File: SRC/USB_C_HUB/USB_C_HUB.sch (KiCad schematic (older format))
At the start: 44 parts, among them J1 USB_C_Receptacle, J2 USB3_A, J3 USB3_A, J4 USB_C_Receptacle, P1 USB_C_Plug, P2 USB_C_Plug_USB2.0, U1 HD3SS460, U2 SY6280, U3 SY6280, U4 SY6280, U5 SY6280

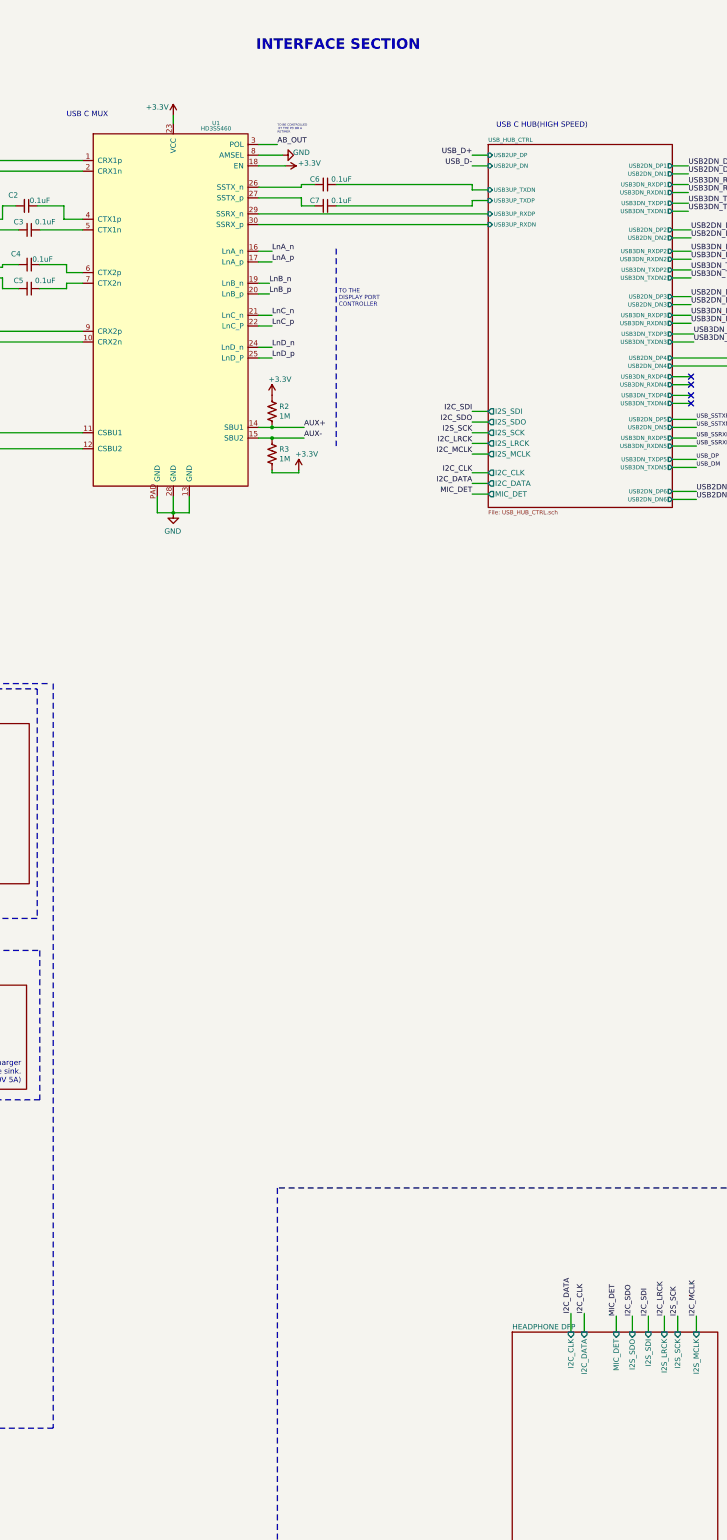
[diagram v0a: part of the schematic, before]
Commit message: schematic capture complete. Pending FULL Footprint assignment. accetable warnings=21
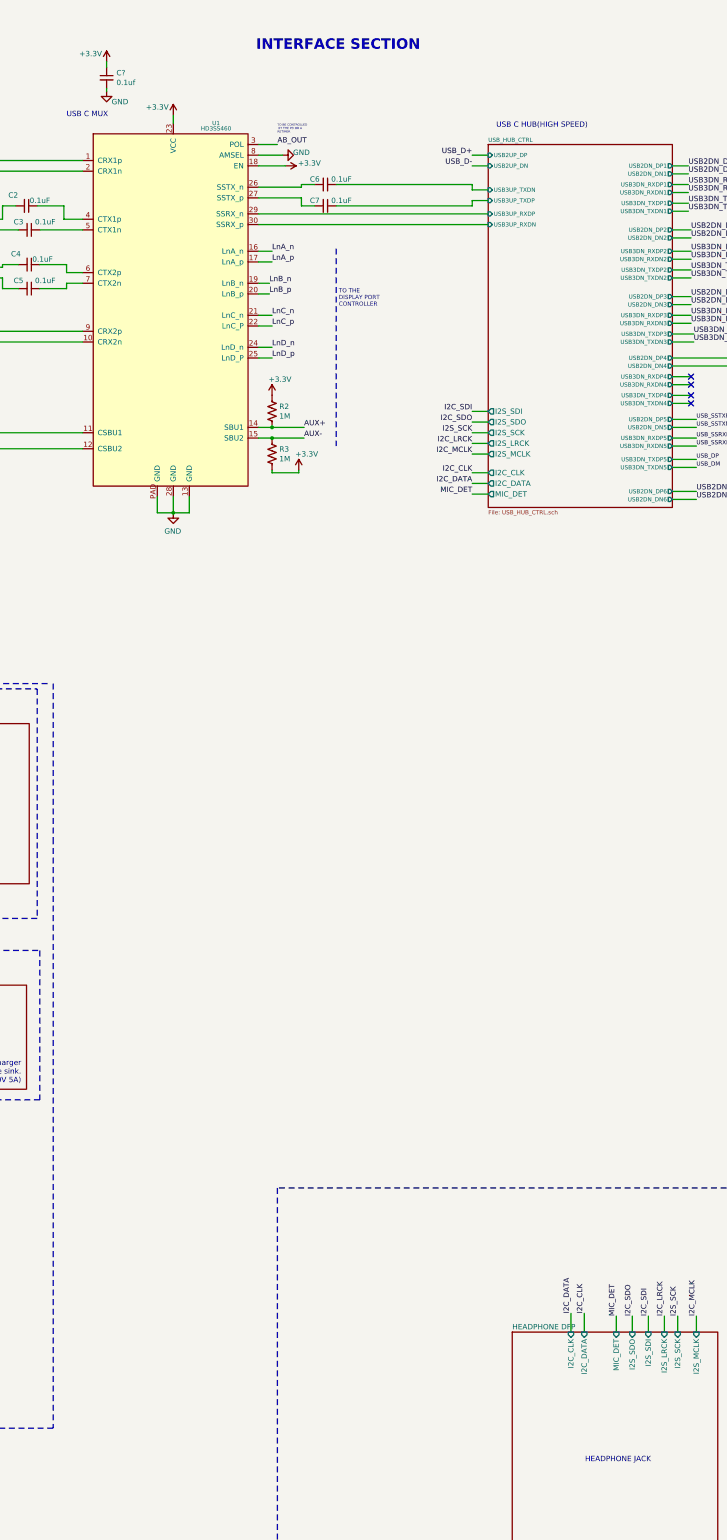
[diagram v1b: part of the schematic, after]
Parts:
- added C?: 0.1uf, symbol Device:C_Small
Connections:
- net +3V3: now also C?.1
- net GND: now also C?.2
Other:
- note added: "HEADPHONE JACK\n"
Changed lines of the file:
@@
 encoding utf-8
 Sheet 1 15
-Title ""
-Date ""
-Rev ""
+Title "USB C HUB"
+Date "2021-10-28"
+Rev "1.1"
 Comp ""
-Comment1 ""
+Comment1 "Designer: ROBERT M M"
 Comment2 ""
 Comment3 ""
@@
 Wire Notes Line
 	15650 525  15650 11575
+$Comp
+L Device:C_Small C?
+U 1 1 64CB2E8E
+P 6425 1175
+F 0 "C?" H 6517 1221 50  0000 L CNN
+F 1 "0.1uf" H 6517 1130 50  0000 L CNN
+F 2 "" H 6425 1175 50  0001 C CNN
+F 3 "~" H 6425 1175 50  0001 C CNN
+	1    6425 1175
+	1    0    0    -1
+$EndComp
+$Comp
+L OLIMEX_Power:+3.3V #PWR?
+U 1 1 64CB3D37
+P 6425 1025
+F 0 "#PWR?" H 6425 875 50  0001 C CNN
+F 1 "+3.3V" H 6275 1100 50  0000 C CNN
+F 2 "" H 6425 1025 60  0000 C CNN
+F 3 "" H 6425 1025 60  0000 C CNN
+	1    6425 1025
+	1    0    0    -1
+$EndComp
+$Comp
+L OLIMEX_Power:GND #PWR?
+U 1 1 64CDC8A5
+P 6425 1300
+AR Path="/619540C6/64CDC8A5" Ref="#PWR?"  Part="1"
+AR Path="/64CDC8A5" Ref="#PWR?"  Part="1"
+F 0 "#PWR?" H 6425 1050 50  0001 C CNN
+F 1 "GND" H 6300 1200 50  0000 C CNN
+F 2 "" H 6425 1300 60  0000 C CNN
+F 3 "" H 6425 1300 60  0000 C CNN
+	1    6425 1300
+	-1   0    0    -1
+$EndComp
+Wire Wire Line
+	6425 1025 6425 1075
+Wire Wire Line
+	6425 1275 6425 1300
+Text Notes 11525 14150 2    50   ~ 0
+HEADPHONE JACK\n
 $EndSCHEMATC

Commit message: schematic capture and footprint assignment complete. Pending approval
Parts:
- removed P2: USB_C_Plug_USB2.0, symbol Connector:USB_C_Plug_USB2.0
- added J10: USB_C_Receptacle_USB2.0, footprints:GCT_USB4105_REVA, symbol Connector:USB_C_Receptacle_USB2.0
- C1, C12: footprint (none) -> Capacitor_SMD:C_0402_1005Metric; Mfr No. (none) -> 0402B104K6R3CT
- C10, C11, C13, C17, C19, C8: footprint (none) -> Capacitor_SMD:C_0603_1608Metric
- C14, C16, C18, C2, C3, C4, C5, C6, C7: footprint (none) -> Capacitor_SMD:C_0402_1005Metric
- C15, C9: footprint (none) -> Capacitor_SMD:C_0603_1608Metric; Mfr No. (none) -> CL10A106MQ8NNNC
- C203: renamed from C?; footprint (none) -> Capacitor_SMD:C_0402_1005Metric
- J1: footprint (none) -> Connector_USB:USB_C_Receptacle_Amphenol_12401610E4-2A
- J2, J3: footprint (none) -> footprints:USB_A_3.1_GCT_USB1075-XX-X-X_REVE
- J4: footprint (none) -> footprints:usb_C_MOLEX_105450-0101
- P1: footprint (none) -> footprints:USB_C_PLUG_GCT_USB4155-03-C_REVA
- R1: value R_US -> 1K; footprint (none) -> Resistor_SMD:R_0402_1005Metric; Mfr No. (none) -> 0402WGF1001TCE
- R2: footprint (none) -> Resistor_SMD:R_0402_1005Metric; Mfr No, (none) -> 0402WGF1004TCE
- R3: footprint (none) -> Resistor_SMD:R_0402_1005Metric
- R4: footprint (none) -> Resistor_SMD:R_0603_1608Metric; Mfr No. (none) -> AS03W4J0682T5E
- R5, R6, R7: footprint (none) -> Resistor_SMD:R_0603_1608Metric
- U1: footprint (none) -> footprints:QFN40P450X250X80-31N120X320
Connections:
- net GND: now also J10.A1 (GND), J10.A12 (GND), J10.B1 (GND), J10.B12 (GND), J10.S1 (SHIELD)
- net USB2DN_DN6: now also J10.A7 (D-)
- net USB2DN_DP6: now also J10.A6 (D+)
- net at C13.1, C18.1, U2.1 (OUT): now also J10.A4 (VBUS), J10.A9 (VBUS), J10.B4 (VBUS), J10.B9 (VBUS)
- no-connect marks 30 -> 32

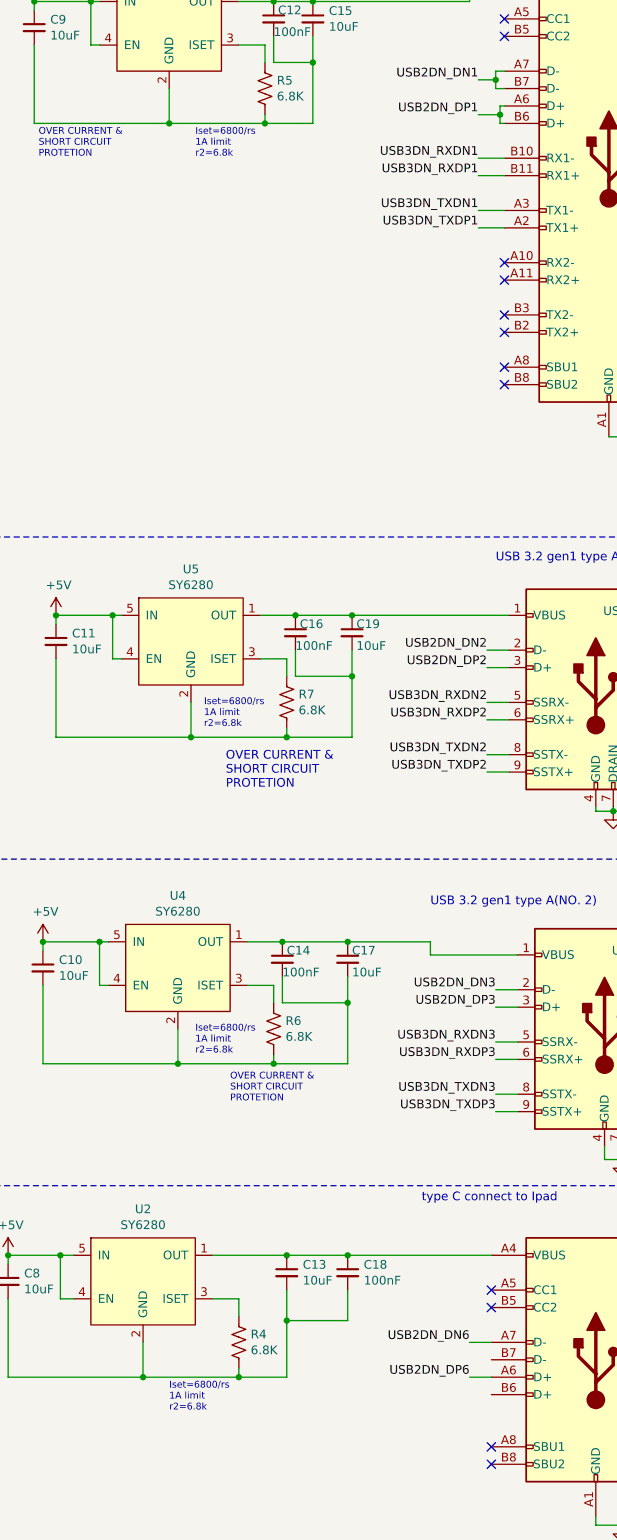
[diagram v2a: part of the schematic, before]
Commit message: schematic capture and footprint assignment complete.
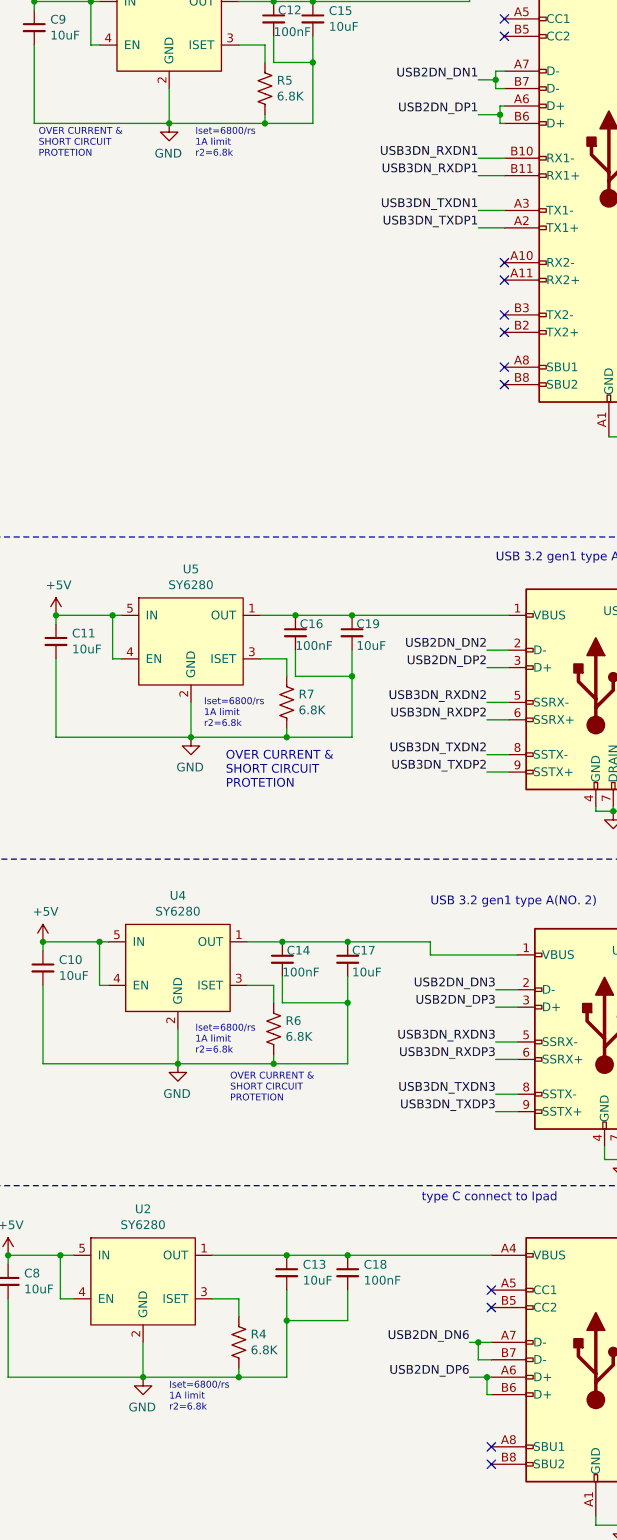
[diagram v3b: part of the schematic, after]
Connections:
- net GND: now also C10.2, C11.2, C12.2, C13.2, C14.2, C15.2, C16.2, C17.2, C18.2, C19.2, C8.2, C9.2, R4.2, R5.2, R6.2, R7.2, U2.2 (GND), U3.2 (GND), U4.2 (GND), U5.2 (GND)
- net USB2DN_DN6: now also J10.B7 (D-)
- net USB2DN_DP6: now also J10.B6 (D+)
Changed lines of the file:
@@
 USB2DN_DN6
 Wire Wire Line
-	21425 8650 21300 8650
-Wire Wire Line
-	21425 8850 21300 8850
+	21425 8650 21350 8650
 NoConn ~ 21425 8450
 NoConn ~ 21425 8350
@@
 NoConn ~ 21425 9250
 NoConn ~ 21425 9350
+$Comp
+L OLIMEX_Power:GND #PWR?
+U 1 1 617FB915
+P 19575 1650
+AR Path="/619540C6/617FB915" Ref="#PWR?"  Part="1"
+AR Path="/617FB915" Ref="#PWR0206"  Part="1"
+F 0 "#PWR0206" H 19575 1400 50  0001 C CNN
+F 1 "GND" H 19580 1477 50  0000 C CNN
+F 2 "" H 19575 1650 60  0000 C CNN
+F 3 "" H 19575 1650 60  0000 C CNN
+	1    19575 1650
+	-1   0    0    -1
+$EndComp
+$Comp
+L OLIMEX_Power:GND #PWR?
+U 1 1 61824BB1
+P 19700 5175
+AR Path="/619540C6/61824BB1" Ref="#PWR?"  Part="1"
+AR Path="/61824BB1" Ref="#PWR0207"  Part="1"
+F 0 "#PWR0207" H 19700 4925 50  0001 C CNN
+F 1 "GND" H 19705 5002 50  0000 C CNN
+F 2 "" H 19700 5175 60  0000 C CNN
+F 3 "" H 19700 5175 60  0000 C CNN
+	1    19700 5175
+	-1   0    0    -1
+$EndComp
+$Comp
+L OLIMEX_Power:GND #PWR?
+U 1 1 61876F90
+P 19625 7050
+AR Path="/619540C6/61876F90" Ref="#PWR?"  Part="1"
+AR Path="/61876F90" Ref="#PWR0208"  Part="1"
+F 0 "#PWR0208" H 19625 6800 50  0001 C CNN
+F 1 "GND" H 19630 6877 50  0000 C CNN
+F 2 "" H 19625 7050 60  0000 C CNN
+F 3 "" H 19625 7050 60  0000 C CNN
+	1    19625 7050
+	-1   0    0    -1
+$EndComp
+$Comp
+L OLIMEX_Power:GND #PWR?
+U 1 1 618C95D5
+P 19425 8850
+AR Path="/619540C6/618C95D5" Ref="#PWR?"  Part="1"
+AR Path="/618C95D5" Ref="#PWR0209"  Part="1"
+F 0 "#PWR0209" H 19425 8600 50  0001 C CNN
+F 1 "GND" H 19430 8677 50  0000 C CNN
+F 2 "" H 19425 8850 60  0000 C CNN
+F 3 "" H 19425 8850 60  0000 C CNN
+	1    19425 8850
+	-1   0    0    -1
+$EndComp
+Wire Wire Line
+	21425 8750 21350 8750
+Wire Wire Line
+	21350 8750 21350 8650
+Connection ~ 21350 8650
+Wire Wire Line
+	21350 8650 21300 8650
+Wire Wire Line
+	21400 8850 21400 8950
+Wire Wire Line
+	21400 8950 21425 8950
+Wire Wire Line
+	21300 8850 21400 8850
+Connection ~ 21400 8850
+Wire Wire Line
+	21400 8850 21425 8850
 $EndSCHEMATC
